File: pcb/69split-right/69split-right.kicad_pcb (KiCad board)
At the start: 2 copper layers, 186.1 x 105.3 mm, 84 parts, among them J1 Conn_01x03_Socket, J2 USB_C_Receptacle_USB2.0_16P, SW1 &,7,,F7, SW10 I, SW11 O, SW12 P, SW13 {,[, SW14 },], SW15 Enter, SW16 Delete,Insert, SW17 H, SW18 J, SW19 K, SW2 *,8,,F8, SW20 L, SW21 :,;, SW22 @,', SW23 #,~, SW24 Home,PgUp, SW25 N, SW26 M, SW27 <,,, SW28 >,., SW29 ?,/, SW3 (,9,,F9, SW30 Shift, SW31 ↑, SW32 End,PgDn, SW33 Space, SW34 Alt,`,¬, SW35 Fn, SW36 Ctrl, SW37 ←, SW38 ↓, SW39 →, SW4 ),0,,F10, SW5 _,-,,F11, SW6 +,=,,F12, SW7 Backspace, SW8 Y, SW9 U, U1 MCP23017_SS

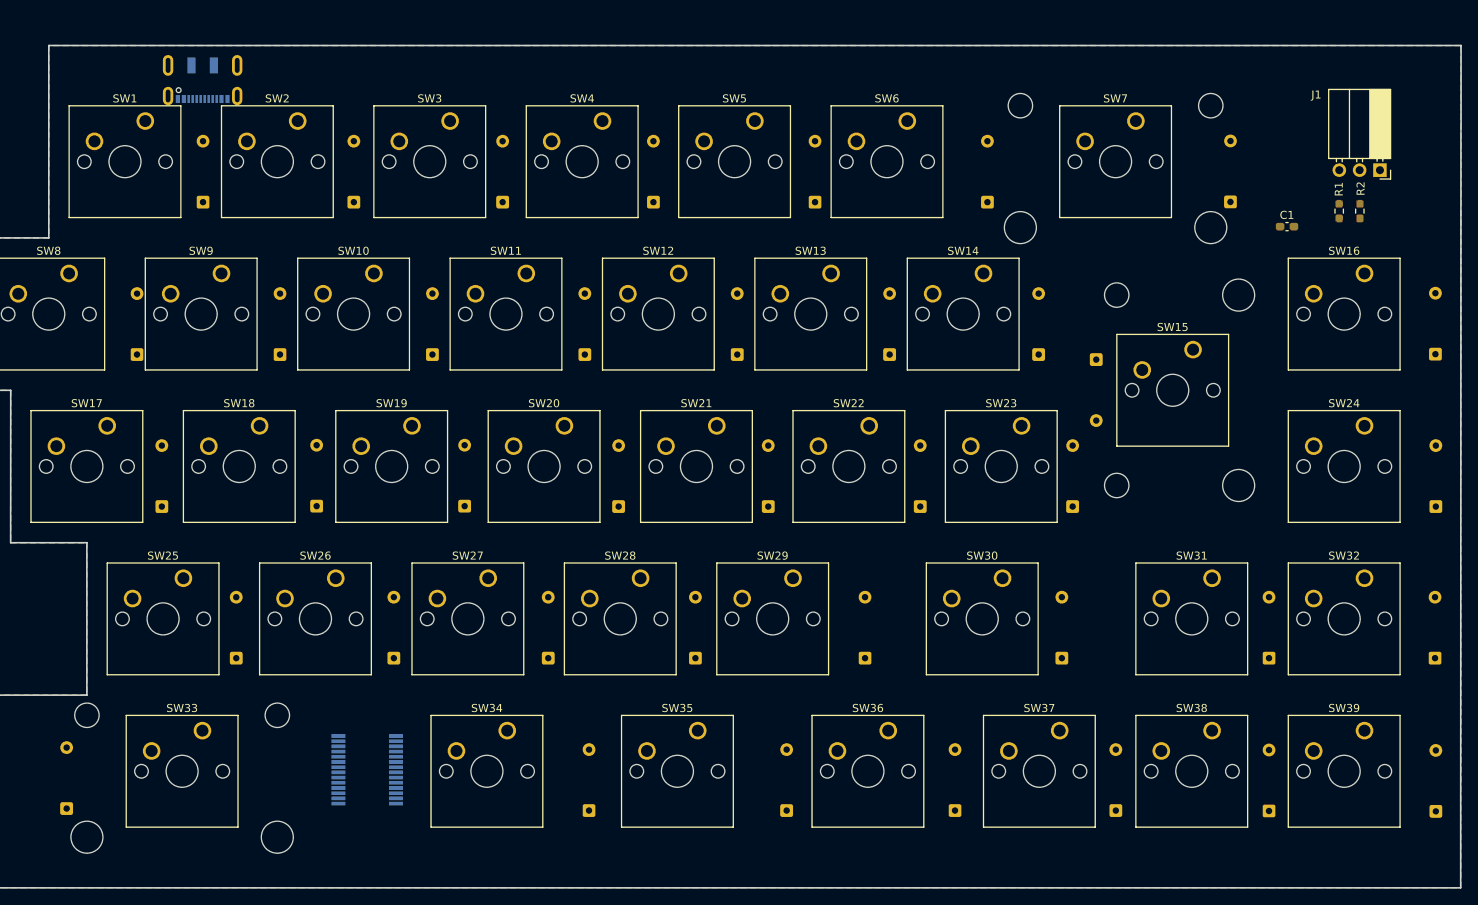
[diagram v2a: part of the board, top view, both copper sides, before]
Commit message: Minor improvements to left schematic and layout.
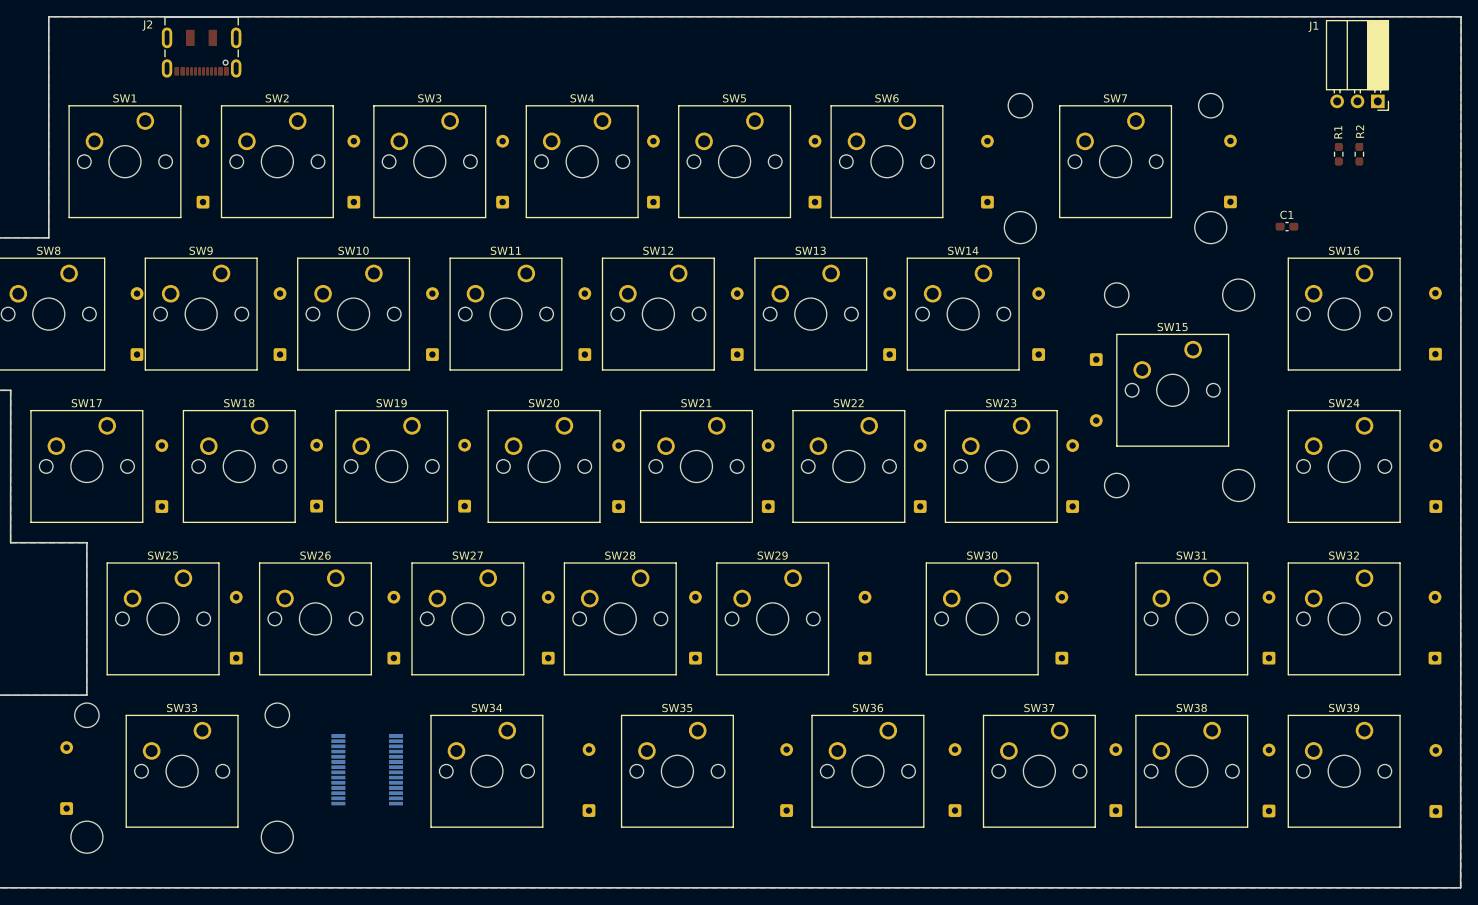
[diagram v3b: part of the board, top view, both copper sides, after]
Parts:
- J2: moved to F.Cu
- moved J1 8.60 mm to (230.1, 51.0)
- moved R1 7.12 mm to (225.2, 57.7)
- moved R2 7.12 mm to (227.8, 57.7)
- moved J2 3.45 mm to (83.0, 44.3), turned to 180 degrees
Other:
- board size 186.1 x 105.3 mm -> 186.1 x 108.9 mm

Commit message: Alright I think now the left side is actually ready.
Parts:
- U1: moved to F.Cu
- moved U1 144.1 mm to (227.3, 60.5)
- moved D33 29.9 mm to (96.0, 139.4)
- moved R1 10.2 mm to (233.8, 49.5), turned to -90 degrees
- moved R2 8.60 mm to (221.4, 49.9)
- moved C1 4.62 mm to (221.3, 62.9), turned to -90 degrees
- renumbered D9 to D10, D10 to D11, D11 to D12, D12 to D13, D13 to D14, D14 to D15, D15 to D16, D16 to D8, D8 to D9, R2 to R1, R1 to R2, SW9 to SW10, SW10 to SW11, SW11 to SW12, SW12 to SW13, SW13 to SW14, SW14 to SW15, SW15 to SW16, SW16 to SW8, SW8 to SW9
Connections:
- D1 pad 1: /Right Matrix/ROW0 -> /IO Expander/ROW0
- D10 pad 1: /Right Matrix/ROW1 -> /IO Expander/ROW1
- D11 pad 1: /Right Matrix/ROW1 -> /IO Expander/ROW1
- D12 pad 1: /Right Matrix/ROW1 -> /IO Expander/ROW1
- D13 pad 1: /Right Matrix/ROW1 -> /IO Expander/ROW1
- D14 pad 1: /Right Matrix/ROW1 -> /IO Expander/ROW1
- D15 pad 1: /Right Matrix/ROW1 -> /IO Expander/ROW1
- D16 pad 1: /Right Matrix/ROW1 -> /IO Expander/ROW1
- D17 pad 1: /Right Matrix/ROW2 -> /IO Expander/ROW2
- D18 pad 1: /Right Matrix/ROW2 -> /IO Expander/ROW2
- D19 pad 1: /Right Matrix/ROW2 -> /IO Expander/ROW2
- D2 pad 1: /Right Matrix/ROW0 -> /IO Expander/ROW0
- D20 pad 1: /Right Matrix/ROW2 -> /IO Expander/ROW2
- D21 pad 1: /Right Matrix/ROW2 -> /IO Expander/ROW2
- D22 pad 1: /Right Matrix/ROW2 -> /IO Expander/ROW2
- D23 pad 1: /Right Matrix/ROW2 -> /IO Expander/ROW2
- D24 pad 1: /Right Matrix/ROW2 -> /IO Expander/ROW2
- D25 pad 1: /Right Matrix/ROW3 -> /IO Expander/ROW3
- D26 pad 1: /Right Matrix/ROW3 -> /IO Expander/ROW3
- D27 pad 1: /Right Matrix/ROW3 -> /IO Expander/ROW3
- D28 pad 1: /Right Matrix/ROW3 -> /IO Expander/ROW3
- D29 pad 1: /Right Matrix/ROW3 -> /IO Expander/ROW3
- D3 pad 1: /Right Matrix/ROW0 -> /IO Expander/ROW0
- D30 pad 1: /Right Matrix/ROW3 -> /IO Expander/ROW3
- D31 pad 1: /Right Matrix/ROW3 -> /IO Expander/ROW3
- D32 pad 1: /Right Matrix/ROW3 -> /IO Expander/ROW3
- D33 pad 1: /Right Matrix/ROW4 -> /IO Expander/ROW4
- D34 pad 1: /Right Matrix/ROW4 -> /IO Expander/ROW4
- D35 pad 1: /Right Matrix/ROW4 -> /IO Expander/ROW4
- D36 pad 1: /Right Matrix/ROW4 -> /IO Expander/ROW4
- D37 pad 1: /Right Matrix/ROW4 -> /IO Expander/ROW4
- D38 pad 1: /Right Matrix/ROW4 -> /IO Expander/ROW4
- D39 pad 1: /Right Matrix/ROW4 -> /IO Expander/ROW4
- D4 pad 1: /Right Matrix/ROW0 -> /IO Expander/ROW0
- D5 pad 1: /Right Matrix/ROW0 -> /IO Expander/ROW0
- D6 pad 1: /Right Matrix/ROW0 -> /IO Expander/ROW0
- D7 pad 1: /Right Matrix/ROW0 -> /IO Expander/ROW0
- D8 pad 1: /Right Matrix/ROW1 -> /IO Expander/ROW0
- D9 pad 1: /Right Matrix/ROW1 -> /IO Expander/ROW1
- R1 pad 2: Net-(J1-Pin_2) -> Net-(J1-Pin_3)
- R2 pad 2: Net-(J1-Pin_3) -> Net-(J1-Pin_2)
- SW24 pad 1: /IO Expander/COL14 -> /IO Expander/COL13
- SW25 pad 1: /IO Expander/COL7 -> /IO Expander/COL6
- SW26 pad 1: /IO Expander/COL8 -> /IO Expander/COL7
- SW27 pad 1: /IO Expander/COL9 -> /IO Expander/COL8
- SW28 pad 1: /IO Expander/COL10 -> /IO Expander/COL9
- SW29 pad 1: /IO Expander/COL11 -> /IO Expander/COL10
- SW30 pad 1: /IO Expander/COL12 -> /IO Expander/COL11
- SW31 pad 1: /IO Expander/COL13 -> /IO Expander/COL12
- SW32 pad 1: /IO Expander/COL14 -> /IO Expander/COL13
- SW33 pad 1: /IO Expander/COL7 -> /IO Expander/COL6
- SW34 pad 1: /IO Expander/COL9 -> /IO Expander/COL8
- SW35 pad 1: /IO Expander/COL10 -> /IO Expander/COL9
- SW36 pad 1: /IO Expander/COL11 -> /IO Expander/COL10
- SW37 pad 1: /IO Expander/COL12 -> /IO Expander/COL11
- SW38 pad 1: /IO Expander/COL13 -> /IO Expander/COL12
- SW39 pad 1: /IO Expander/COL14 -> /IO Expander/COL13
- SW7 pad 1: /IO Expander/COL13 -> /IO Expander/COL12
- SW8 pad 1: /IO Expander/COL14 -> /IO Expander/COL13
- U1 pad 1: unconnected-(U1-GPB0-Pad1) -> /IO Expander/ROW0
- U1 pad 2: unconnected-(U1-GPB1-Pad2) -> /IO Expander/ROW1
- U1 pad 21: unconnected-(U1-GPA0-Pad21) -> /IO Expander/COL6
- U1 pad 22: unconnected-(U1-GPA1-Pad22) -> /IO Expander/COL7
- U1 pad 23: unconnected-(U1-GPA2-Pad23) -> /IO Expander/COL8
- U1 pad 24: unconnected-(U1-GPA3-Pad24) -> /IO Expander/COL9
- U1 pad 25: unconnected-(U1-GPA4-Pad25) -> /IO Expander/COL10
- U1 pad 26: unconnected-(U1-GPA5-Pad26) -> /IO Expander/COL11
- U1 pad 27: unconnected-(U1-GPA6-Pad27) -> /IO Expander/COL12
- U1 pad 28: unconnected-(U1-GPA7-Pad28) -> /IO Expander/COL13
- U1 pad 3: unconnected-(U1-GPB2-Pad3) -> /IO Expander/ROW2
- U1 pad 4: unconnected-(U1-GPB3-Pad4) -> /IO Expander/ROW3
- U1 pad 5: unconnected-(U1-GPB4-Pad5) -> /IO Expander/ROW4
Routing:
- net /IO Expander/COL12: track 0.00 -> 115.4 mm
- net /IO Expander/COL11: track 0.00 -> 92.0 mm
- net /IO Expander/COL10: track 0.00 -> 91.0 mm
- net /IO Expander/COL9: track 0.00 -> 89.5 mm
- net /IO Expander/COL8: track 0.00 -> 87.0 mm
- net /IO Expander/COL6: track 0.00 -> 87.0 mm
- net /IO Expander/COL13: track 0.00 -> 78.6 mm
- net /IO Expander/COL7: track 0.00 -> 67.0 mm
- net /IO Expander/ROW0: track 0.00 -> 4.14 mm
- net Net-(D32-A): track 0.00 -> 1.94 mm

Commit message: First draft of the right side.
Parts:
- added J3: Conn_01x03_Socket, Connector_PinSocket_2.54mm:PinSocket_1x03_P2.54mm_Horizontal, F.Cu at (234.3, 51.0)
- added R10: 330R, Resistor_SMD:R_0603_1608Metric_Pad0.98x0.95mm_HandSolder, F.Cu at (238.2, 48.1)
- added R11: 330R, Resistor_SMD:R_0603_1608Metric_Pad0.98x0.95mm_HandSolder, F.Cu at (238.2, 52.0)
- added R3: 1k, Resistor_SMD:R_0603_1608Metric_Pad0.98x0.95mm_HandSolder, F.Cu at (219.1, 66.9)
- added R4: 1k, Resistor_SMD:R_0603_1608Metric_Pad0.98x0.95mm_HandSolder, F.Cu at (223.6, 66.9)
- added R8: 1k, Resistor_SMD:R_0603_1608Metric_Pad0.98x0.95mm_HandSolder, F.Cu at (233.5, 64.0)
- added R9: 330R, Resistor_SMD:R_0603_1608Metric_Pad0.98x0.95mm_HandSolder, F.Cu at (238.2, 44.3)
- SW1: value &,7,,F7 -> SW_Push
- SW10: value U -> SW_Push
- SW11: value I -> SW_Push
- SW12: value O -> SW_Push
- SW13: value P -> SW_Push
- SW14: value {,[ -> SW_Push
- SW15: value },] -> SW_Push
- SW16: value Enter -> SW_Push
- SW17: value H -> SW_Push
- SW18: value J -> SW_Push
- SW19: value K -> SW_Push
- SW2: value *,8,,F8 -> SW_Push
- SW20: value L -> SW_Push
- SW21: value :,; -> SW_Push
- SW22: value @,' -> SW_Push
- SW23: value #,~ -> SW_Push
- SW24: value Home,PgUp -> SW_Push
- SW25: value N -> SW_Push
- SW26: value M -> SW_Push
- SW27: value <,, -> SW_Push
- SW28: value >,. -> SW_Push
- SW29: value ?,/ -> SW_Push
- SW3: value (,9,,F9 -> SW_Push
- SW30: value Shift -> SW_Push
- SW31: value ↑ -> SW_Push
- SW32: value End,PgDn -> SW_Push
- SW33: value Space -> SW_Push
- SW34: value Alt,`,¬ -> SW_Push
- SW35: value Fn -> SW_Push
- SW36: value Ctrl -> SW_Push
- SW37: value ← -> SW_Push
- SW38: value ↓ -> SW_Push
- SW39: value → -> SW_Push
- SW4: value ),0,,F10 -> SW_Push
- SW5: value _,-,,F11 -> SW_Push
- SW6: value +,=,,F12 -> SW_Push
- SW7: value Backspace -> SW_Push
- SW8: value Delete,Insert -> SW_Push
- SW9: value Y -> SW_Push
- moved R1 29.6 mm to (205.3, 41.8), turned to 180 degrees
- moved R2 12.4 mm to (212.1, 41.8), turned to 0 degrees
- moved D16 9.03 mm to (195.0, 92.4), turned to 90 degrees
- moved J1 4.56 mm to (225.5, 51.0)
- moved C1 2.26 mm to (219.7, 61.3), turned to 180 degrees
- moved D7 0.59 mm to (211.1, 63.6)
- moved D33 0.22 mm to (96.0, 139.6)
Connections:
- R1 pad 1: /GPIO Outputs/GPIO_OUT_PB7 -> Net-(J1-Pin_3)
- R1 pad 2: Net-(J1-Pin_3) -> /GPIO Outputs/GPIO_OUT_PB7
- U1 pad 12: /IO Expander/SCK -> /IO Expander/SCL
- U1 pad 15: unconnected-(U1-A0-Pad15) -> GND
- U1 pad 16: unconnected-(U1-A1-Pad16) -> GND
- U1 pad 17: unconnected-(U1-A2-Pad17) -> GND
- U1 pad 18: unconnected-(U1-~{RESET}-Pad18) -> Net-(U1-~{RESET})
- U1 pad 6: unconnected-(U1-GPB5-Pad6) -> /GPIO Outputs/GPB5
- U1 pad 7: unconnected-(U1-GPB6-Pad7) -> /GPIO Outputs/GPB6
- U1 pad 8: unconnected-(U1-GPB7-Pad8) -> /GPIO Outputs/GPB7
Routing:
- net /IO Expander/COL6: track 87.0 -> 323.1 mm, vias 0 -> 6
- net /IO Expander/ROW4: track 0.00 -> 233.9 mm, vias 0 -> 4
- net /IO Expander/ROW3: track 0.00 -> 222.0 mm, vias 0 -> 3
- net /IO Expander/ROW2: track 0.00 -> 217.7 mm, vias 0 -> 5
- net /IO Expander/COL7: track 67.0 -> 275.7 mm, vias 0 -> 6
- net /IO Expander/ROW1: track 0.13 -> 197.8 mm, vias 0 -> 5
- net /IO Expander/ROW0: track 4.14 -> 200.6 mm, vias 0 -> 5
- net VCC: track 0.00 -> 190.9 mm, vias 0 -> 6
- net /IO Expander/COL8: track 87.0 -> 271.3 mm, vias 0 -> 6
- net /IO Expander/SDA: track 0.00 -> 171.1 mm, vias 0 -> 6
- net /IO Expander/SCL: track 0.00 -> 167.2 mm, vias 0 -> 6
- net /GPIO Outputs/GPIO_OUT_PB6: track 0.00 -> 154.7 mm, vias 0 -> 8
- net /GPIO Outputs/GPIO_OUT_PB7: track 0.00 -> 153.6 mm, vias 0 -> 4
- net /IO Expander/COL10: track 91.0 -> 234.1 mm, vias 0 -> 7
- net /IO Expander/COL11: track 92.0 -> 229.7 mm, vias 0 -> 7
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
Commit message: I think the right side is done???. Added image and 3D files.
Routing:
- net /GPIO Outputs/GPB7: track 28.4 -> 29.4 mm
- net /IO Expander/ROW3: track 222.0 -> 221.3 mm
- net /GPIO Outputs/GPB5: track 32.8 -> 32.2 mm
- net /IO Expander/COL11: track 229.7 -> 229.2 mm
- net GND: vias 24 -> 28

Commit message: Finished design and layout?
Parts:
- moved J1 0.22 mm to (225.5, 50.8)
- moved J3 0.22 mm to (234.2, 50.8)
- moved U1 0.07 mm to (227.2, 60.5)
- moved D13 0.05 mm to (149.9, 82.7)
- moved D16 0.05 mm to (195.0, 92.4)
- moved D21 0.05 mm to (153.8, 101.7)
- moved D22 0.05 mm to (172.8, 101.7)
- moved D25 0.05 mm to (87.3, 120.7)
- moved D27 0.05 mm to (126.3, 120.7)
- moved D28 0.05 mm to (144.7, 120.7)
- moved D29 0.05 mm to (165.9, 120.7)
- moved D31 0.05 mm to (216.4, 120.7)
- moved D32 0.05 mm to (237.2, 120.7)
- moved D34 0.05 mm to (131.4, 139.7)
- moved D36 0.05 mm to (177.2, 139.7)
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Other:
- outline, holes or cut-outs redrawn
- board text added: "2LEFT"
- board text added: "69SPLIT"
- board text added: "GND"
- board text added: "GPB5"
- board text added: "GPB6"
- board text added: "GPB7"
- board text added: "PB6"
- board text added: "PB7"

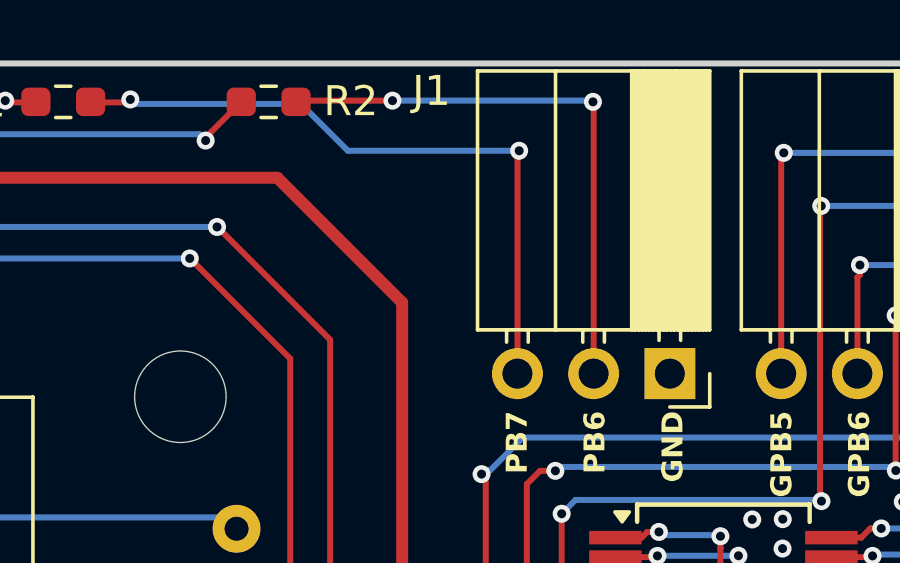
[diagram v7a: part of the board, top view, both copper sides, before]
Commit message: Added silkscreen for ATmega and MCP pins.
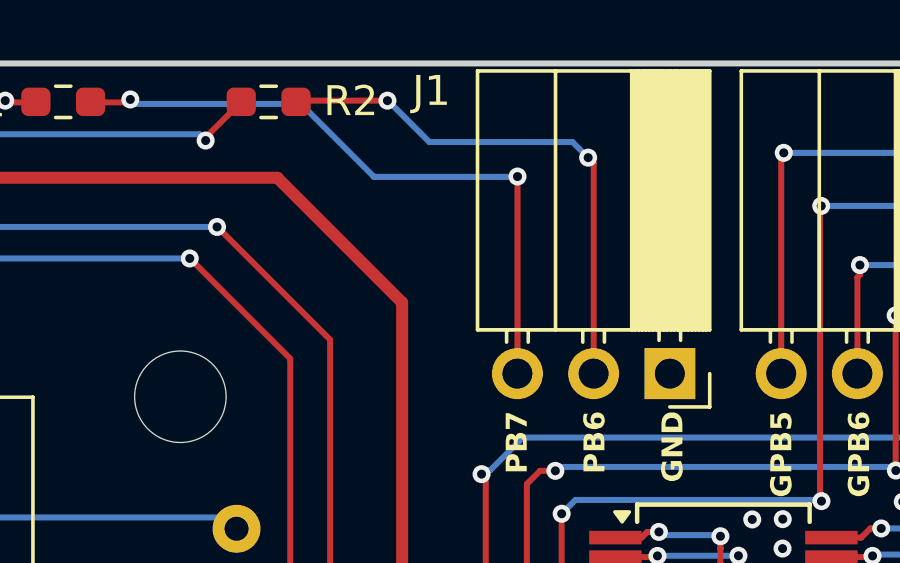
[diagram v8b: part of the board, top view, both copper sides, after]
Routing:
- net Net-(J1-Pin_2): track 19.2 -> 18.1 mm
- net Net-(J1-Pin_3): track 22.7 -> 22.1 mm
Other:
- board text added: "ATMEGA32U4 PINS"
- board text added: "MCP23017 PINS"
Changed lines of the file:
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@@
+		)
+	)
+	(gr_text "MCP23017\nPINS"
+		(at 231.68 42.76 0)
+		(layer "B.SilkS" knockout)
+		(effects
+			(font
+				(size 0.7 0.7)
+				(thickness 0.12)
+			)
+			(justify bottom mirror)
+		)
+	)
+	(gr_text "ATMEGA32U4\nPINS"
+		(at 222.91 42.78 0)
+		(layer "B.SilkS" knockout)
+		(effects
+			(font
+				(size 0.7 0.7)
+				(thickness 0.12)
+			)
+			(justify bottom mirror)
 		)
 	)
@@
 	)
 	(segment
-		(start 220.43 43.39)
-		(end 220.375 43.445)
+		(start 207.37 41.78)
+		(end 206.145 41.78)
 		(width 0.2)
 		(layer "F.Cu")
@@
 	)
 	(segment
-		(start 220.375 43.445)
+		(start 220.375 44.25)
 		(end 220.375 51.03)
 		(width 0.2)
@@
 		(net 40)
 	)
-	(segment
-		(start 207.37 41.78)
-		(end 206.145 41.78)
-		(width 0.2)
-		(layer "F.Cu")
-		(net 40)
-	)
 	(via
-		(at 220.43 43.39)
+		(at 220.375 44.25)
 		(size 0.6)
 		(drill 0.3)
@@
 	)
 	(segment
+		(start 220.375 44.25)
+		(end 220.365 44.26)
+		(width 0.2)
+		(layer "B.Cu")
+		(net 40)
+	)
+	(segment
+		(start 220.365 44.26)
+		(end 215.59 44.26)
+		(width 0.2)
+		(layer "B.Cu")
+		(net 40)
+	)
+	(segment
 		(start 207.62 41.83)
 		(end 207.47 41.68)
@@
 	)
 	(segment
-		(start 220.43 43.39)
-		(end 214.72 43.39)
-		(width 0.2)
-		(layer "B.Cu")
-		(net 40)
-	)
-	(segment
 		(start 213.16 41.83)
 		(end 207.62 41.83)
@@
 	)
 	(segment
-		(start 214.72 43.39)
+		(start 215.59 44.26)
 		(end 213.16 41.83)
 		(width 0.2)
@@
 	)
 	(segment
-		(start 216.207355 41.72)
-		(end 213.1675 41.72)
+		(start 213.1 41.6525)
+		(end 213.1 41.78)
 		(width 0.2)
 		(layer "F.Cu")
@@
 	)
 	(segment
-		(start 222.89 41.76)
-		(end 222.915 41.785)
+		(start 216.04 41.72)
+		(end 213.1675 41.72)
 		(width 0.2)
 		(layer "F.Cu")
@@
 	)
 	(segment
-		(start 213.1 41.6525)
-		(end 213.1 41.78)
+		(start 213.1675 41.72)
+		(end 213.1 41.6525)
 		(width 0.2)
 		(layer "F.Cu")
@@
 	)
 	(segment
-		(start 222.915 41.785)
+		(start 222.915 43.805)
 		(end 222.915 51.03)
 		(width 0.2)
@@
 	)
 	(segment
-		(start 213.1675 41.72)
-		(end 213.1 41.6525)
+		(start 222.73 43.62)
+		(end 222.915 43.805)
 		(width 0.2)
 		(layer "F.Cu")
@@
 	)
 	(via
-		(at 222.89 41.76)
+		(at 222.73 43.62)
 		(size 0.6)
 		(drill 0.3)
@@
 	)
 	(via
-		(at 216.207355 41.72)
+		(at 216.04 41.72)
 		(size 0.6)
 		(drill 0.3)
@@
 	)
 	(segment
-		(start 216.207355 41.72)
-		(end 222.76 41.72)
+		(start 216.04 41.72)
+		(end 216.06 41.72)
 		(width 0.2)
 		(layer "B.Cu")
@@
 	)
 	(segment
-		(start 222.8 41.76)
-		(end 222.89 41.76)
+		(start 217.44 43.1)
+		(end 222.21 43.1)
 		(width 0.2)
 		(layer "B.Cu")
@@
 	)
 	(segment
-		(start 222.76 41.72)
-		(end 222.8 41.76)
-		(width 0.2)
-		(layer "B.Cu")
+		(start 216.06 41.72)
+		(end 217.44 43.1)
+		(width 0.2)
+		(layer "B.Cu")
+		(net 41)
+	)
+	(segment
+		(start 222.21 43.1)
+		(end 222.73 43.62)
+		(width 0.2)
+		(layer "B.Cu")
